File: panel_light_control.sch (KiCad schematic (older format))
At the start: 77 parts, among them J1 Conn_01x02, J6 Conn_01x04, Q1 IRF540N, Q2 IRF540N, Q3 IRF540N, U1 L7805, U2 LM324

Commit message: pinout validated against CubeMX listing (.ioc added), some nets renamed, system RGB LED reconnected. Reconnected I2C lines to include CAN alternate function. Warning: * bottom silkscreen labels might be invalidated
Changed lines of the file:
@@
-	1    0    0    -1
-$EndComp
-$Comp
-L power:PWR_FLAG #FLG0102
-U 1 1 5D0841CC
-P 1050 1600
-F 0 "#FLG0102" H 1050 1675 50  0001 C CNN
-F 1 "PWR_FLAG" H 1050 1773 50  0000 C CNN
-F 2 "" H 1050 1600 50  0001 C CNN
-F 3 "~" H 1050 1600 50  0001 C CNN
-	1    1050 1600
 	1    0    0    -1
 $EndComp
@@
 	1700 1700 1700 1900
 Wire Wire Line
-	1300 1700 1050 1700
-Wire Wire Line
-	1050 1700 1050 1600
-Connection ~ 1300 1700
-$Comp
-L power:PWR_FLAG #FLG0103
-U 1 1 5C1B04BB
-P 4300 800
-F 0 "#FLG0103" H 4300 875 50  0001 C CNN
-F 1 "PWR_FLAG" H 4300 974 50  0000 C CNN
-F 2 "" H 4300 800 50  0001 C CNN
-F 3 "~" H 4300 800 50  0001 C CNN
-	1    4300 800
-	1    0    0    -1
-$EndComp
-$Comp
-L power:PWR_FLAG #FLG0104
-U 1 1 5C1C5DD8
-P 6150 1100
-F 0 "#FLG0104" H 6150 1175 50  0001 C CNN
-F 1 "PWR_FLAG" H 6150 1274 50  0000 C CNN
-F 2 "" H 6150 1100 50  0001 C CNN
-F 3 "~" H 6150 1100 50  0001 C CNN
-	1    6150 1100
-	1    0    0    -1
-$EndComp
-$Comp
-L power:PWR_FLAG #FLG0105
-U 1 1 5C227DE5
-P 4300 2250
-F 0 "#FLG0105" H 4300 2325 50  0001 C CNN
-F 1 "PWR_FLAG" H 4300 2424 50  0000 C CNN
-F 2 "" H 4300 2250 50  0001 C CNN
-F 3 "~" H 4300 2250 50  0001 C CNN
-	1    4300 2250
-	1    0    0    -1
-$EndComp
-Wire Wire Line
-	4300 2250 4300 2350
-Connection ~ 4300 2350
-Wire Wire Line
 	4550 900  4300 900
 Connection ~ 4300 900
@@
 Wire Wire Line
 	8200 3000 8200 3100
-Wire Wire Line
-	6150 1100 6150 1200
 Connection ~ 6150 1200
 Wire Wire Line
@@
 Wire Wire Line
 	3200 2350 3300 2350
-Wire Wire Line
-	4300 800  4300 900
 $Comp
 L Device:LED_RCBG D?
@@
 	6150 1550 6150 1700
 Connection ~ 5850 1700
+$Comp
+L power:PWR_FLAG #FLG0103
+U 1 1 5BF52E34
+P 3000 1100
+F 0 "#FLG0103" H 3000 1175 50  0001 C CNN
+F 1 "PWR_FLAG" H 3000 1274 50  0000 C CNN
+F 2 "" H 3000 1100 50  0001 C CNN
+F 3 "~" H 3000 1100 50  0001 C CNN
+	1    3000 1100
+	1    0    0    -1
+$EndComp
+Wire Wire Line
+	3000 1100 3000 1200
+$Comp
+L power:PWR_FLAG #FLG0104
+U 1 1 5BF8FE53
+P 3300 2250
+F 0 "#FLG0104" H 3300 2325 50  0001 C CNN
+F 1 "PWR_FLAG" H 3300 2424 50  0000 C CNN
+F 2 "" H 3300 2250 50  0001 C CNN
+F 3 "~" H 3300 2250 50  0001 C CNN
+	1    3300 2250
+	1    0    0    -1
+$EndComp
+Wire Wire Line
+	3300 2250 3300 2350
+Connection ~ 1300 1700
+Wire Wire Line
+	1300 1700 1050 1700
+Wire Wire Line
+	1050 1700 1050 1600
+$Comp
+L power:PWR_FLAG #FLG0102
+U 1 1 5D0841CC
+P 1050 1600
+F 0 "#FLG0102" H 1050 1675 50  0001 C CNN
+F 1 "PWR_FLAG" H 1050 1773 50  0000 C CNN
+F 2 "" H 1050 1600 50  0001 C CNN
+F 3 "~" H 1050 1600 50  0001 C CNN
+	1    1050 1600
+	1    0    0    -1
+$EndComp
 $EndSCHEMATC

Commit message: final touches: add fiducials for PCBA
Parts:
- added FID1, FID2, FID3, FID4, FID5, FID6: Fiducial, Fiducial:Fiducial_1mm_Dia_2.54mm_Outer_CopperTop, symbol Connector:TestPoint
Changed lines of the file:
@@
+	1    0    0    -1
+$EndComp
+$Comp
+L Connector:TestPoint FID1
+U 1 1 5BE3B736
+P 5450 6600
+F 0 "FID1" H 5508 6718 50  0000 L CNN
+F 1 "Fiducial" H 5508 6627 50  0000 L CNN
+F 2 "Fiducial:Fiducial_1mm_Dia_2.54mm_Outer_CopperTop" H 5650 6600 50  0001 C CNN
+F 3 "~" H 5650 6600 50  0001 C CNN
+	1    5450 6600
+	1    0    0    -1
+$EndComp
+$Comp
+L Connector:TestPoint FID2
+U 1 1 5BE3EE88
+P 5450 6800
+F 0 "FID2" H 5508 6918 50  0000 L CNN
+F 1 "Fiducial" H 5508 6827 50  0000 L CNN
+F 2 "Fiducial:Fiducial_1mm_Dia_2.54mm_Outer_CopperTop" H 5650 6800 50  0001 C CNN
+F 3 "~" H 5650 6800 50  0001 C CNN
+	1    5450 6800
+	1    0    0    -1
+$EndComp
+$Comp
+L Connector:TestPoint FID3
+U 1 1 5BE40FE9
+P 5450 7000
+F 0 "FID3" H 5508 7118 50  0000 L CNN
+F 1 "Fiducial" H 5508 7027 50  0000 L CNN
+F 2 "Fiducial:Fiducial_1mm_Dia_2.54mm_Outer_CopperTop" H 5650 7000 50  0001 C CNN
+F 3 "~" H 5650 7000 50  0001 C CNN
+	1    5450 7000
+	1    0    0    -1
+$EndComp
+$Comp
+L Connector:TestPoint FID4
+U 1 1 5BE41C23
+P 5450 7200
+F 0 "FID4" H 5508 7318 50  0000 L CNN
+F 1 "Fiducial" H 5508 7227 50  0000 L CNN
+F 2 "Fiducial:Fiducial_1mm_Dia_2.54mm_Outer_CopperTop" H 5650 7200 50  0001 C CNN
+F 3 "~" H 5650 7200 50  0001 C CNN
+	1    5450 7200
+	1    0    0    -1
+$EndComp
+$Comp
+L Connector:TestPoint FID5
+U 1 1 5BE434C9
+P 5450 7400
+F 0 "FID5" H 5508 7518 50  0000 L CNN
+F 1 "Fiducial" H 5508 7427 50  0000 L CNN
+F 2 "Fiducial:Fiducial_1mm_Dia_2.54mm_Outer_CopperTop" H 5650 7400 50  0001 C CNN
+F 3 "~" H 5650 7400 50  0001 C CNN
+	1    5450 7400
+	1    0    0    -1
+$EndComp
+$Comp
+L Connector:TestPoint FID6
+U 1 1 5BE45F4A
+P 5450 7600
+F 0 "FID6" H 5508 7718 50  0000 L CNN
+F 1 "Fiducial" H 5508 7627 50  0000 L CNN
+F 2 "Fiducial:Fiducial_1mm_Dia_2.54mm_Outer_CopperTop" H 5650 7600 50  0001 C CNN
+F 3 "~" H 5650 7600 50  0001 C CNN
+	1    5450 7600
 	1    0    0    -1
 $EndComp

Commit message: BOM DONE
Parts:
- C1, C8, C9: value 1uF -> 2.2uF; MPN (none) -> 885012106011; Mouser (none) -> 710-885012106011
- C10, C11, C4: MPN (none) -> C0603C103K1REAUTO; Mouser (none) -> 80-C0603C103K1REAUTO
- C12, C13, C14, C16, C38, C39, C40, C44, C45, C46, C5, C6, C7: MPN (none) -> C0603C104K5RECAUTO; Mouser (none) -> 80-C0603C104K5REAUTO
- C47: MPN (none) -> GRM21BR71A475KE51L; Mouser (none) -> 81-GRM21BR71A475KE1L
- D12: MPN (none) -> 1N4004-T; Mouser (none) -> 621-1N4004
- I2C1: MPN S4B-PH-K-S(LF)(SN)‎ -> S4B-PH-K-S(LF)(SN)‎
- J1: DigiKey (none) -> 455-1719-ND; MPN (none) -> S2B-PH-K-S(LF)(SN)‎
- J6: DigiKey 455-1721-ND‎ -> (none); MPN S4B-PH-K-S(LF)(SN) -> 31320104; Manufacturer (none) -> RIA CONNECT; Reichelt (none) -> AKL 320-04
- PANEL2: Mouser 490-PJ-063AH -> 490-PJ-063AH
- PS1, PS2: MPN (none) -> LDD-1000H
- PS12: MPN (none) -> R-78B12-2.0
- R1, R7, R9: value 30k -> 33k; MPN (none) -> RC0603FR-0733KL; Mouser (none) -> 603-RC0603FR-0733KL
- R10, R2, R8: MPN (none) -> RC0603FR-072K2L; Mouser (none) -> 603-RC0603FR-072K2L
- R11, R12, R3: MPN (none) -> RC0603FR-074M7L; Mouser (none) -> 603-RC0603FR-074M7L
- R13, R15, R4: value 100 -> 120R; MPN (none) -> RC0603FR-07120RL; Mouser (none) -> 603-RC0603FR-07120RL
- R14, R16, R5: value 2k -> 2.2k; MPN (none) -> RC0603FR-072K2L; Mouser (none) -> 603-RC0603FR-072K2L
- R39: value 220R -> 120R; MPN (none) -> RC0603FR-07120RL; Mouser (none) -> 603-RC0603FR-07120RL
- R40, R41: MPN (none) -> RC0603FR-071KL; Mouser (none) -> 603-RC0603FR-071KL
- U1: MPN (none) -> L7805CV; Mouser (none) -> 511-L7805CV
- U2: MPN (none) -> LM324ADR; Mouser (none) -> 595-LM324ADR

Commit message: BOM completed, inventory checked and listed in BOM. Adds project diagram.
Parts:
- C10, C11, C12, C13, C14, C16, C25, C3, C38, C39, C4, C40, C41, C42, C43, C44, C45, C46, C47, C5, C6, C7, DBG1, FID1, FID2, FID3, FID4, FID5, FID6, H1, H2, H3, H4, I2C1, JTAG1, R1, R10, R13, R14, R15, R16, R2, R39, R4, R40, R41, R5, R7, R8, R9, SPI0, SPI1, UART1: stock (none) -> X
- D12, Q1, Q2, Q3, U1: stock (none) -> (X)
- J1: DigiKey 455-1719-ND -> (none); MPN S2B-PH-K-S(LF)(SN)‎ -> 31320102; Reichelt (none) -> AKL 320-04
- PS1, PS2: stock (none) -> (2)

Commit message: PLCC-4 RGB LEDs LED9 and LED10 are the wrong parts (common cathode required, part is common anode and different input). Fix: source 0606 LEDs (metric 1616) - RD1616-63RGBC-C2CA or DL-PCB0606RGBC-C2. Require switching to Broadcom ASMB-TTF0-0A20B in next revision (uncommitted, can be configured as common cathode, available on Mouser)
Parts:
- C1, C8, C9: MPN 885012106011 -> C0603C225K9RACTU; Mouser 710-885012106011 -> 80-C0603C225K9R; box no (none) -> 4
- C10, C11, C4: box no (none) -> 5
- C12, C13, C14, C16, C38, C39, C40, C44, C45, C46, C5, C6, C7: box no (none) -> 2
- C25, C3, C41, C42, C43, DBG1, FID1, FID2, FID3, FID4, FID5, FID6, H1, H2, H3, H4, I2C1, JTAG1, SPI0, SPI1, UART1: box no (none) -> E
- C47: box no (none) -> 3
- D12, U1: stock (X) -> (none)
- J1: Mouser (none) -> 571-796644-2; Reichelt AKL 320-04 -> AKL 320-02
- LED10: MPN ASMB-KTF0-0A306 -> RD1616-63RGBC-C2CA or DL-PCB0606RGBC-C2; Mouser 630-ASMB-KTF0-0A306 -> 630-ASMB-KTF0-0A306 (WRONG PART)
- PS1, PS2: stock (2) -> (none)
- Q1, Q2, Q3: box no (none) -> E; stock (X) -> X
- R1, R7, R9: box no (none) -> 16
- R10, R14, R16, R2, R5, R8: box no (none) -> 17
- R13, R15, R39, R4: box no (none) -> 18
- R40, R41: box no (none) -> 21
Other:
- note added: "WRONG PART\nNEXT REV: 630-ASMB-TTF0-0A20B"

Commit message: restored MCO1 = 25 MHz, PHY blinking pattern changed (SPEED on permanently, ACT fast blinking, RMII-RXDn activity) but TXEN only stays high for 6µs max. No SMI activity within 100ms after that.
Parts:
- C1, C10, C11, C12, C13, C14, C16, C25, C3, C38, C39, C4, C40, C41, C42, C43, C44, C45, C46, C5, C6, C7, C8, C9: symbol Device:C -> panel_light_control-rescue:C-Device
- C47: symbol Device:C_Small -> panel_light_control-rescue:C_Small-Device
- D1, D2, D4: symbol Device:D -> panel_light_control-rescue:D-Device
- D12: symbol Diode:1N4001 -> panel_light_control-rescue:1N4001-Diode
- DBG1: symbol Connector_Generic:Conn_01x06 -> panel_light_control-rescue:Conn_01x06-Connector_Generic
- F1: symbol Device:Polyfuse_Small -> panel_light_control-rescue:Polyfuse_Small-Device
- FID1, FID2, FID3, FID4, FID5, FID6: symbol Connector:TestPoint -> panel_light_control-rescue:TestPoint-Connector
- H1, H2, H3, H4: symbol Mechanical:MountingHole -> panel_light_control-rescue:MountingHole-Mechanical
- I2C1, J6, UART1: symbol Connector_Generic:Conn_01x04 -> panel_light_control-rescue:Conn_01x04-Connector_Generic
- J1: symbol Connector_Generic:Conn_01x02 -> panel_light_control-rescue:Conn_01x02-Connector_Generic
- JTAG1, SPI1: symbol Connector_Generic:Conn_01x07 -> panel_light_control-rescue:Conn_01x07-Connector_Generic
- L2, L3: symbol Device:L -> panel_light_control-rescue:L-Device
- LED10: symbol Device:LED_RCBG -> panel_light_control-rescue:LED_RCBG-Device
- PANEL1, PANEL2: symbol Connector_Generic_MountingPin:Conn_01x02_MountingPin -> panel_light_control-rescue:Conn_01x02_MountingPin-Connector_Generic_MountingPin
- PS12: symbol Regulator_Switching:R-78B12-2.0 -> panel_light_control-rescue:R-78B12-2.0-Regulator_Switching
- PS33: symbol Regulator_Switching:R-78B3.3-2.0 -> panel_light_control-rescue:R-78B3.3-2.0-Regulator_Switching
- Q1, Q2, Q3: symbol Transistor_FET:IRF540N -> panel_light_control-rescue:IRF540N-Transistor_FET
- R1, R10, R11, R12, R13, R14, R15, R16, R17, R18, R2, R3, R4, R5, R6, R7, R8, R9: symbol Device:R -> panel_light_control-rescue:R-Device
- R39, R40, R41: symbol Device:R_Small -> panel_light_control-rescue:R_Small-Device
- SPI0: symbol Connector_Generic:Conn_01x10 -> panel_light_control-rescue:Conn_01x10-Connector_Generic
- U1: symbol Regulator_Linear:L7805 -> panel_light_control-rescue:L7805-Regulator_Linear
- U2: symbol Amplifier_Operational:LM324 -> panel_light_control-rescue:LM324-Amplifier_Operational

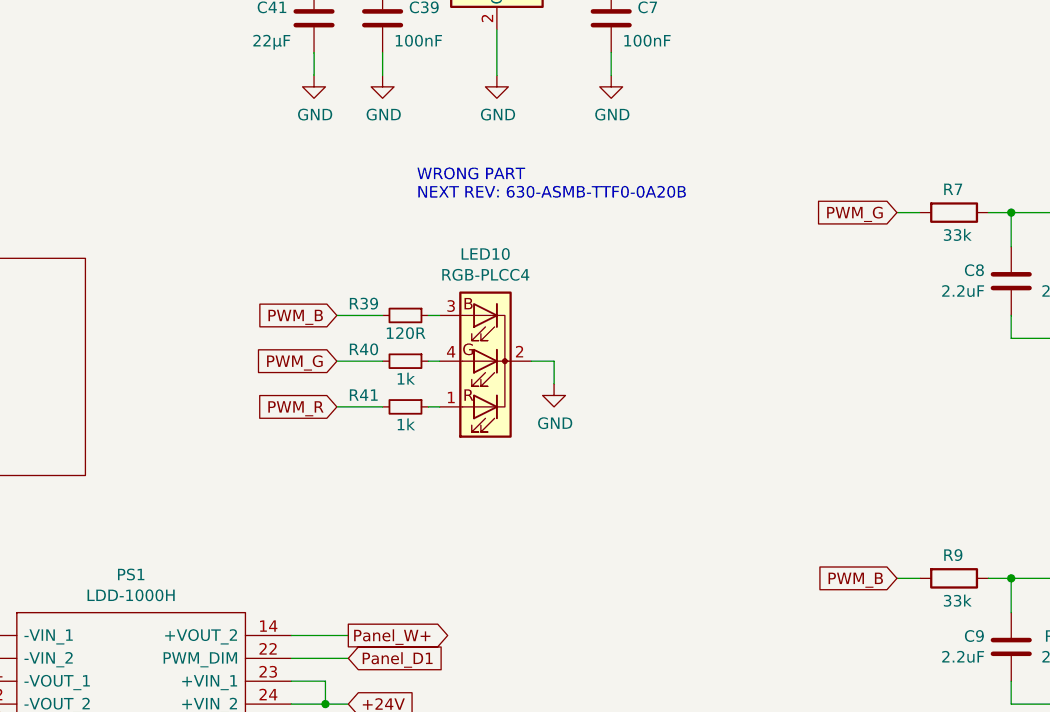
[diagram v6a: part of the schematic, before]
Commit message: Update for v0.2. Revise schematic and PCB layout. See dev log.
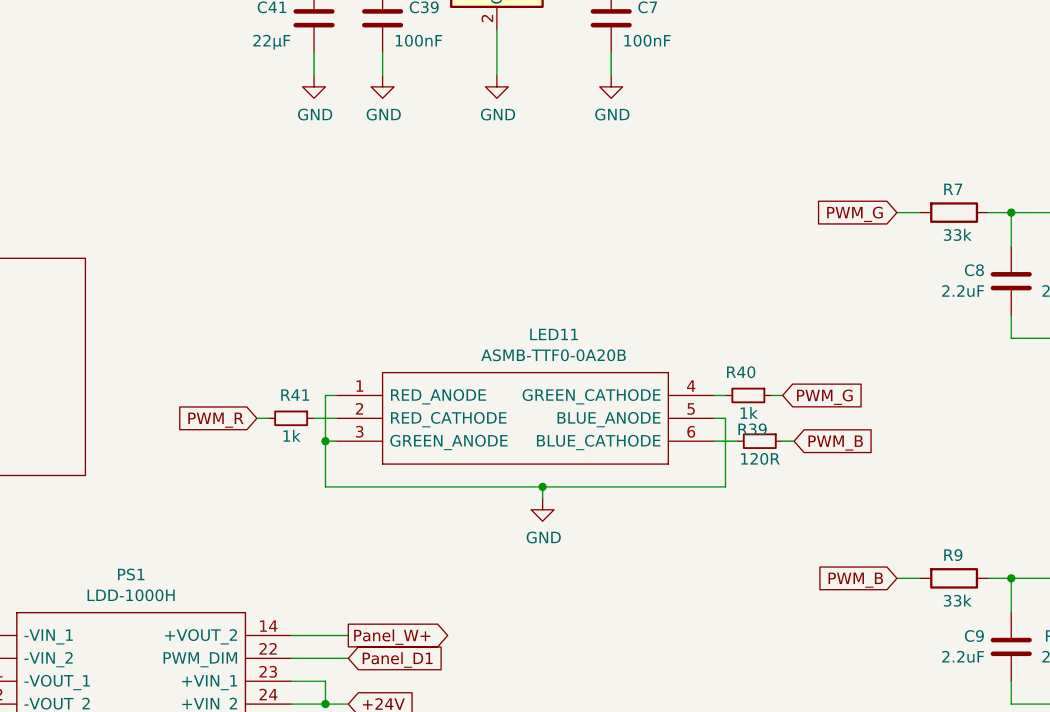
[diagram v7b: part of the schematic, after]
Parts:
- removed LED10: RGB-PLCC4, LED_SMD:LED_Cree-PLCC4_2x2mm_CW, symbol panel_light_control-rescue:LED_RCBG-Device
- added LED11: ASMB-TTF0-0A20B, ASMB-TTF0-0A20B:ASMBTTF00A20B, symbol ASMB-TTF0-0A20B:ASMB-TTF0-0A20B
- R17, R18, R6: MPN RL1220S-R22-F -> KRL1632E-M-R220-F-T5; Mouser 754-RL1220S-R22-F -> 754-KRL1632EMR220FT5
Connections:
- net GND: now also LED11.1 (RED_ANODE), LED11.3 (GREEN_ANODE), LED11.5 (BLUE_ANODE)
- net PWM_B: now also R39.1; no longer R39.2
- net PWM_G: now also R40.1; no longer R40.2
- net at R41.1: now also LED11.2 (RED_CATHODE)
- new net: LED11.4 (GREEN_CATHODE), R40.2
- new net: LED11.6 (BLUE_CATHODE), R39.2
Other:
- note removed: "WRONG PART\nNEXT REV: 630-ASMB-TTF0-0A20B"
- moved on the sheet: R39, R40, R41
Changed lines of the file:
@@
 F 2 "Resistor_SMD:R_1206_3216Metric" V 8130 4400 50  0001 C CNN
 F 3 "~" H 8200 4400 50  0001 C CNN
-F 4 "RL1220S-R22-F" H 8200 4400 50  0001 C CNN "MPN"
-F 5 "754-RL1220S-R22-F" H 8200 4400 50  0001 C CNN "Mouser"
+F 4 "KRL1632E-M-R220-F-T5 " H 8200 4400 50  0001 C CNN "MPN"
+F 5 "754-KRL1632EMR220FT5 " H 8200 4400 50  0001 C CNN "Mouser"
 	1    8200 4400
 	1    0    0    -1
@@
 F 2 "Resistor_SMD:R_1206_3216Metric" V 8130 6000 50  0001 C CNN
 F 3 "~" H 8200 6000 50  0001 C CNN
-F 4 "RL1220S-R22-F" H 8200 6000 50  0001 C CNN "MPN"
-F 5 "754-RL1220S-R22-F" H 8200 6000 50  0001 C CNN "Mouser"
+F 4 "KRL1632E-M-R220-F-T5 " H 8200 6000 50  0001 C CNN "MPN"
+F 5 "754-KRL1632EMR220FT5 " H 8200 6000 50  0001 C CNN "Mouser"
 	1    8200 6000
 	1    0    0    -1
@@
 F 2 "Resistor_SMD:R_1206_3216Metric" V 8130 2850 50  0001 C CNN
 F 3 "~" H 8200 2850 50  0001 C CNN
-F 4 "RL1220S-R22-F" H 8200 2850 50  0001 C CNN "MPN"
-F 5 "754-RL1220S-R22-F" H 8200 2850 50  0001 C CNN "Mouser"
+F 4 "KRL1632E-M-R220-F-T5" H 8200 2850 50  0001 C CNN "MPN"
+F 5 "754-KRL1632EMR220FT5 " H 8200 2850 50  0001 C CNN "Mouser"
 	1    8200 2850
 	1    0    0    -1
@@
 	3200 2350 3300 2350
 $Comp
-L panel_light_control-rescue:LED_RCBG-Device D?
-U 1 1 5BE88702
-P 3750 4400
-AR Path="/5BBC4BB7/5BE88702" Ref="D?"  Part="1"
-AR Path="/5BE88702" Ref="LED10"  Part="1"
-F 0 "LED10" H 3750 3933 50  0000 C CNN
-F 1 "RGB-PLCC4" H 3750 4024 50  0000 C CNN
-F 2 "LED_SMD:LED_Cree-PLCC4_2x2mm_CW" H 3750 4350 50  0001 C CNN
-F 3 "~" H 3750 4350 50  0001 C CNN
-F 4 "RD1616-63RGBC-C2CA or DL-PCB0606RGBC-C2" H 3750 4400 50  0001 C CNN "MPN"
-F 5 "630-ASMB-KTF0-0A306 (WRONG PART)" H 3750 4400 50  0001 C CNN "Mouser"
-	1    3750 4400
-	-1   0    0    1
-$EndComp
-Wire Wire Line
-	3950 4400 4050 4400
-$Comp
 L panel_light_control-rescue:R_Small-Device R?
 U 1 1 5BE8870C
-P 3400 4600
+P 2900 4650
 AR Path="/5BBC4BB7/5BE8870C" Ref="R?"  Part="1"
 AR Path="/5C1EFDBE/5BE8870C" Ref="R?"  Part="1"
@@
 AR Path="/5C211FC6/5BE8870C" Ref="R?"  Part="1"
 AR Path="/5BE8870C" Ref="R41"  Part="1"
-F 0 "R41" V 3350 4350 50  0000 L CNN
-F 1 "1k" V 3450 4600 50  0000 C TNN
-F 2 "Resistor_SMD:R_0603_1608Metric" H 3400 4600 50  0001 C CNN
-F 3 "~" H 3400 4600 50  0001 C CNN
-F 4 "RC0603FR-071KL" H 0   0   50  0001 C CNN "MPN"
-F 5 "603-RC0603FR-071KL" H 0   0   50  0001 C CNN "Mouser"
-F 6 "X" H 0   0   50  0001 C CNN "stock"
-F 7 "21" H 0   0   50  0001 C CNN "box no"
-	1    3400 4600
+F 0 "R41" V 2800 4600 50  0000 L CNN
+F 1 "1k" V 2950 4650 50  0000 C TNN
+F 2 "Resistor_SMD:R_0603_1608Metric" H 2900 4650 50  0001 C CNN
+F 3 "~" H 2900 4650 50  0001 C CNN
+F 4 "RC0603FR-071KL" H -500 50  50  0001 C CNN "MPN"
+F 5 "603-RC0603FR-071KL" H -500 50  50  0001 C CNN "Mouser"
+F 6 "X" H -500 50  50  0001 C CNN "stock"
+F 7 "21" H -500 50  50  0001 C CNN "box no"
+	1    2900 4650
 	0    1    1    0
 $EndComp
@@
 L panel_light_control-rescue:R_Small-Device R?
 U 1 1 5BE88712
-P 3400 4400
+P 4900 4550
 AR Path="/5BBC4BB7/5BE88712" Ref="R?"  Part="1"
 AR Path="/5C1EFDBE/5BE88712" Ref="R?"  Part="1"
@@
 AR Path="/5C211FC6/5BE88712" Ref="R?"  Part="1"
 AR Path="/5BE88712" Ref="R40"  Part="1"
-F 0 "R40" V 3350 4150 50  0000 L CNN
-F 1 "1k" V 3450 4400 50  0000 C TNN
-F 2 "Resistor_SMD:R_0603_1608Metric" H 3400 4400 50  0001 C CNN
-F 3 "~" H 3400 4400 50  0001 C CNN
-F 4 "RC0603FR-071KL" H 0   0   50  0001 C CNN "MPN"
-F 5 "603-RC0603FR-071KL" H 0   0   50  0001 C CNN "Mouser"
-F 6 "X" H 0   0   50  0001 C CNN "stock"
-F 7 "21" H 0   0   50  0001 C CNN "box no"
-	1    3400 4400
+F 0 "R40" V 4800 4450 50  0000 L CNN
+F 1 "1k" V 4950 4550 50  0000 C TNN
+F 2 "Resistor_SMD:R_0603_1608Metric" H 4900 4550 50  0001 C CNN
+F 3 "~" H 4900 4550 50  0001 C CNN
+F 4 "RC0603FR-071KL" H 1500 150 50  0001 C CNN "MPN"
+F 5 "603-RC0603FR-071KL" H 1500 150 50  0001 C CNN "Mouser"
+F 6 "X" H 1500 150 50  0001 C CNN "stock"
+F 7 "21" H 1500 150 50  0001 C CNN "box no"
+	1    4900 4550
 	0    1    1    0
 $EndComp
@@
 L panel_light_control-rescue:R_Small-Device R?
 U 1 1 5BE88718
-P 3400 4200
+P 4950 4750
 AR Path="/5BBC4BB7/5BE88718" Ref="R?"  Part="1"
 AR Path="/5C1EFDBE/5BE88718" Ref="R?"  Part="1"
@@
 AR Path="/5C211FC6/5BE88718" Ref="R?"  Part="1"
 AR Path="/5BE88718" Ref="R39"  Part="1"
-F 0 "R39" V 3350 3950 50  0000 L CNN
-F 1 "120R" V 3450 4200 50  0000 C TNN
-F 2 "Resistor_SMD:R_0603_1608Metric" H 3400 4200 50  0001 C CNN
-F 3 "~" H 3400 4200 50  0001 C CNN
-F 4 "RC0603FR-07120RL" H 0   0   50  0001 C CNN "MPN"
-F 5 "603-RC0603FR-07120RL" H 0   0   50  0001 C CNN "Mouser"
-F 6 "X" H 0   0   50  0001 C CNN "stock"
-F 7 "18" H 0   0   50  0001 C CNN "box no"
-	1    3400 4200
+F 0 "R39" V 4900 4650 50  0000 L CNN
+F 1 "120R" V 5000 4750 50  0000 C TNN
+F 2 "Resistor_SMD:R_0603_1608Metric" H 4950 4750 50  0001 C CNN
+F 3 "~" H 4950 4750 50  0001 C CNN
+F 4 "RC0603FR-07120RL" H 1550 550 50  0001 C CNN "MPN"
+F 5 "603-RC0603FR-07120RL" H 1550 550 50  0001 C CNN "Mouser"
+F 6 "X" H 1550 550 50  0001 C CNN "stock"
+F 7 "18" H 1550 550 50  0001 C CNN "box no"
+	1    4950 4750
 	0    1    1    0
 $EndComp
-Wire Wire Line
-	3100 4200 3300 4200
-Wire Wire Line
-	3100 4400 3300 4400
-Wire Wire Line
-	3100 4600 3300 4600
-Wire Wire Line
-	3550 4600 3500 4600
-Wire Wire Line
-	3500 4400 3550 4400
-Wire Wire Line
-	3550 4200 3500 4200
 $Comp
 L panel_light_control-rescue:GND-power #PWR0121
 U 1 1 5BE9D0EE
-P 4050 4500
-F 0 "#PWR0121" H 4050 4250 50  0001 C CNN
-F 1 "GND" H 4055 4327 50  0000 C CNN
-F 2 "" H 4050 4500 50  0001 C CNN
-F 3 "" H 4050 4500 50  0001 C CNN
-	1    4050 4500
-	1    0    0    -1
-$EndComp
-Wire Wire Line
-	4050 4400 4050 4500
-Text GLabel 3100 4600 0    50   Input ~ 0
+P 4000 5000
+F 0 "#PWR0121" H 4000 4750 50  0001 C CNN
+F 1 "GND" H 4005 4827 50  0000 C CNN
+F 2 "" H 4000 5000 50  0001 C CNN
+F 3 "" H 4000 5000 50  0001 C CNN
+	1    4000 5000
+	1    0    0    -1
+$EndComp
+Text GLabel 2750 4650 0    50   Input ~ 0
 PWM_R
-Text GLabel 3100 4400 0    50   Input ~ 0
+Text GLabel 5050 4550 2    50   Input ~ 0
 PWM_G
-Text GLabel 3100 4200 0    50   Input ~ 0
+Text GLabel 5100 4750 2    50   Input ~ 0
 PWM_B
 $Comp
@@
 	-1   0    0    1
 $EndComp
-Text Notes 3450 3700 0    50   ~ 0
-WRONG PART\nNEXT REV: 630-ASMB-TTF0-0A20B
+$Comp
+L ASMB-TTF0-0A20B:ASMB-TTF0-0A20B LED11
+U 1 1 5D2B61E5
+P 3100 4550
+F 0 "LED11" H 4050 4815 50  0000 C CNN
+F 1 "ASMB-TTF0-0A20B" H 4050 4724 50  0000 C CNN
+F 2 "ASMB-TTF0-0A20B:ASMBTTF00A20B" H 4850 4650 50  0001 L CNN
+F 3 "https://componentsearchengine.com/Datasheets/1/ASMB-TTF0-0A20B.pdf" H 4850 4550 50  0001 L CNN
+F 4 "BROADCOM LIMITED - ASMB-TTF0-0A20B - LED, RGB, 710/1840/410MCD, PLCC-6" H 4850 4450 50  0001 L CNN "Description"
+F 5 "2" H 4850 4350 50  0001 L CNN "Height"
+F 6 "Avago Technologies" H 4850 4250 50  0001 L CNN "Manufacturer_Name"
+F 7 "ASMB-TTF0-0A20B" H 4850 4150 50  0001 L CNN "Manufacturer_Part_Number"
+F 8 "630-ASMB-TTF0-0A20B" H 4850 4050 50  0001 L CNN "Mouser Part Number"
+F 9 "https://www.mouser.com/Search/Refine.aspx?Keyword=630-ASMB-TTF0-0A20B" H 4850 3950 50  0001 L CNN "Mouser Price/Stock"
+F 10 "" H 4850 3850 50  0001 L CNN "RS Part Number"
+F 11 "" H 4850 3750 50  0001 L CNN "RS Price/Stock"
+	1    3100 4550
+	1    0    0    -1
+$EndComp
+Wire Wire Line
+	3100 4550 3050 4550
+Wire Wire Line
+	3050 4550 3050 4750
+Wire Wire Line
+	3050 4950 4000 4950
+Wire Wire Line
+	4000 4950 4000 5000
+Wire Wire Line
+	3100 4750 3050 4750
+Connection ~ 3050 4750
+Wire Wire Line
+	3050 4750 3050 4950
+Wire Wire Line
+	3100 4650 3000 4650
+Wire Wire Line
+	2800 4650 2750 4650
+Wire Wire Line
+	4750 4550 4800 4550
+Wire Wire Line
+	5000 4550 5050 4550
+Wire Wire Line
+	4750 4650 4800 4650
+Wire Wire Line
+	4800 4650 4800 4950
+Wire Wire Line
+	4800 4950 4000 4950
+Connection ~ 4000 4950
+Wire Wire Line
+	4750 4750 4850 4750
+Wire Wire Line
+	5050 4750 5100 4750
 $EndSCHEMATC
